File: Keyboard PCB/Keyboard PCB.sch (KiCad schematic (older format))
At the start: 15 parts

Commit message: Metidas las librerías acheron
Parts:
- added J?: USB_B_Mini, symbol Connector:USB_B_Mini
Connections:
- wire segments 52 -> 55
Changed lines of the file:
@@
 EESchema Schematic File Version 4
+LIBS:Keyboard PCB-cache
 EELAYER 30 0
 EELAYER END
@@
 Wire Wire Line
 	5250 1050 4900 1050
+$Comp
+L Connector:USB_B_Mini J?
+U 1 1 5D835ABB
+P 3500 1200
+F 0 "J?" H 3557 1667 50  0000 C CNN
+F 1 "USB_B_Mini" H 3557 1576 50  0000 C CNN
+F 2 "" H 3650 1150 50  0001 C CNN
+F 3 "~" H 3650 1150 50  0001 C CNN
+	1    3500 1200
+	1    0    0    -1
+$EndComp
+$Comp
+L power:+5V #PWR?
+U 1 1 5D837687
+P 3900 900
+F 0 "#PWR?" H 3900 750 50  0001 C CNN
+F 1 "+5V" H 3915 1073 50  0000 C CNN
+F 2 "" H 3900 900 50  0001 C CNN
+F 3 "" H 3900 900 50  0001 C CNN
+	1    3900 900
+	1    0    0    -1
+$EndComp
+Text GLabel 3800 1200 2    50   Input ~ 0
+D+
+Text GLabel 3800 1300 2    50   Input ~ 0
+D-
+Wire Wire Line
+	3800 1000 3900 1000
+Wire Wire Line
+	3900 1000 3900 900
+$Comp
+L power:GND #PWR?
+U 1 1 5D83AD54
+P 3500 1800
+F 0 "#PWR?" H 3500 1550 50  0001 C CNN
+F 1 "GND" H 3505 1627 50  0000 C CNN
+F 2 "" H 3500 1800 50  0001 C CNN
+F 3 "" H 3500 1800 50  0001 C CNN
+	1    3500 1800
+	1    0    0    -1
+$EndComp
+Wire Wire Line
+	3500 1600 3500 1800
 $EndSCHEMATC

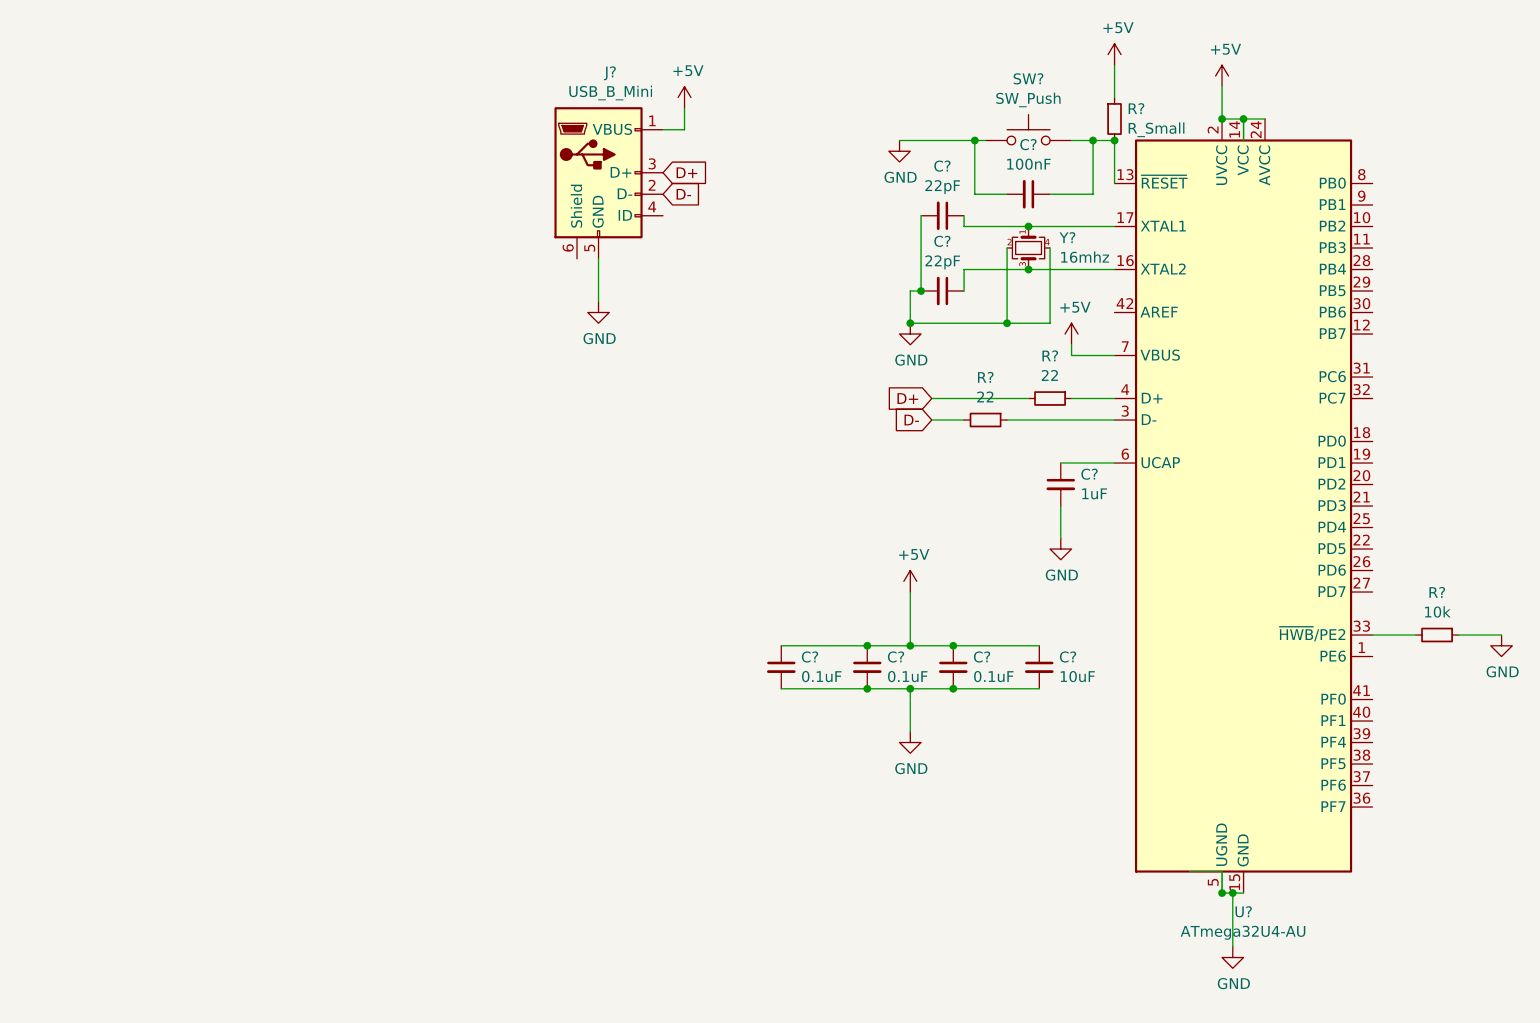
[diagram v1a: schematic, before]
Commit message: Añadida la librería de acheron
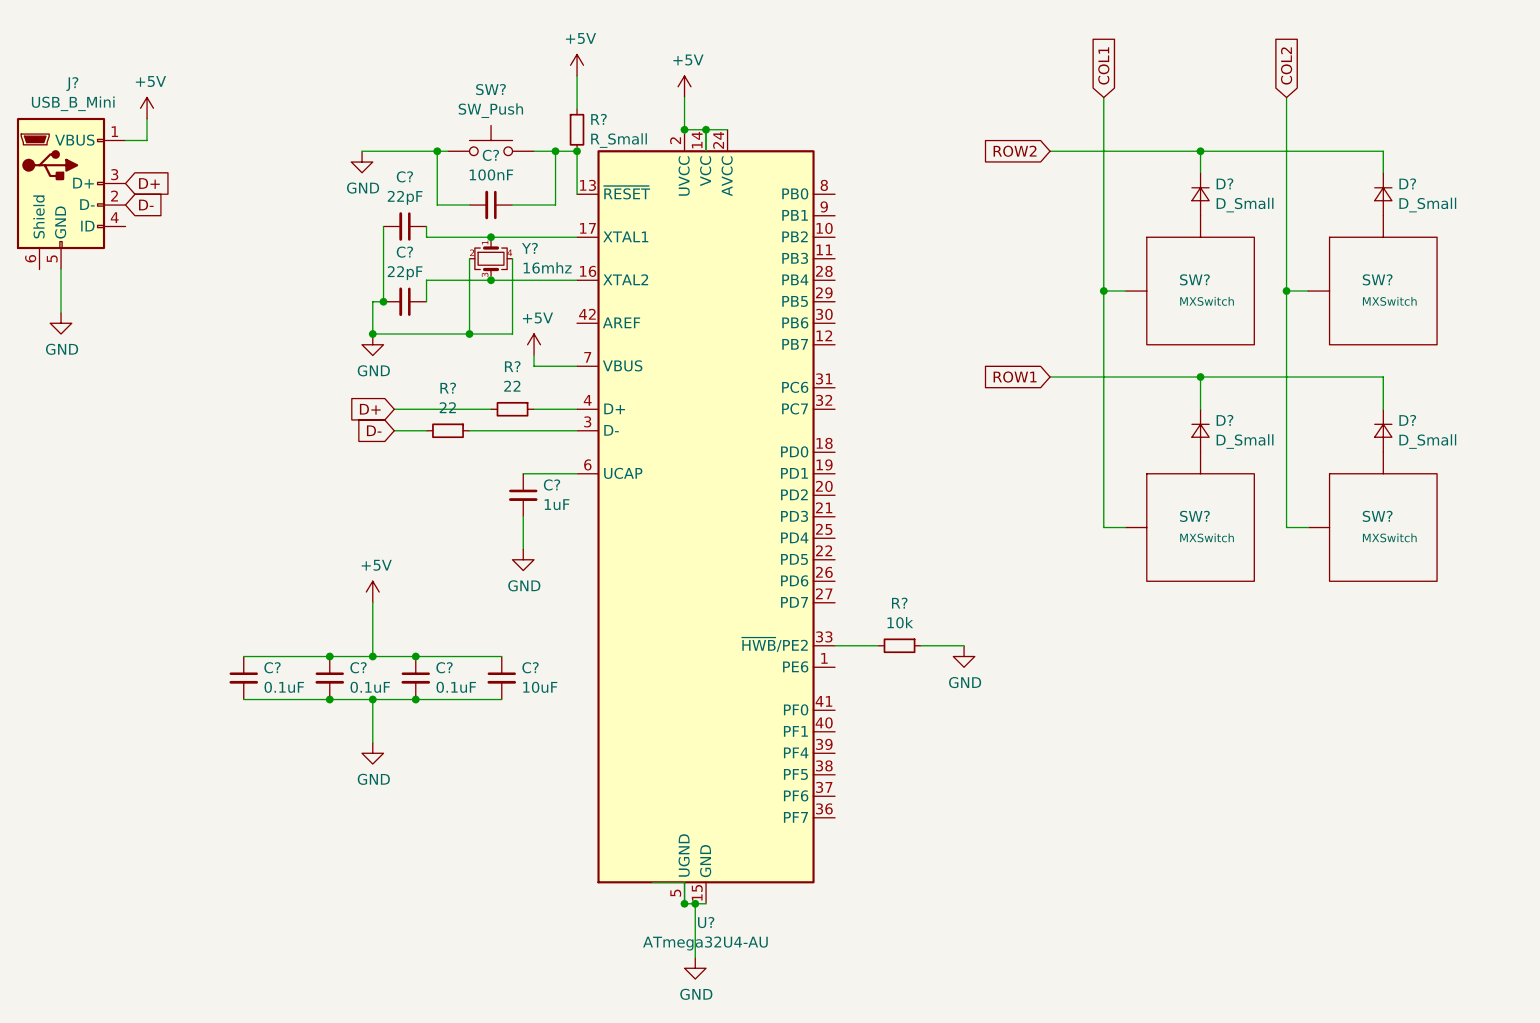
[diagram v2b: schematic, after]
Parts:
- added D? (x4): D_Small, symbol Device:D_Small
- added SW? (x4): MXSwitch, symbol acheronSymbols:MXSwitch
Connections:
- net labels added: COL1, COL2, ROW1, ROW2
- wire segments 55 -> 71
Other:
- moved on the sheet: C?, J?, R?, SW?, U?, Y?

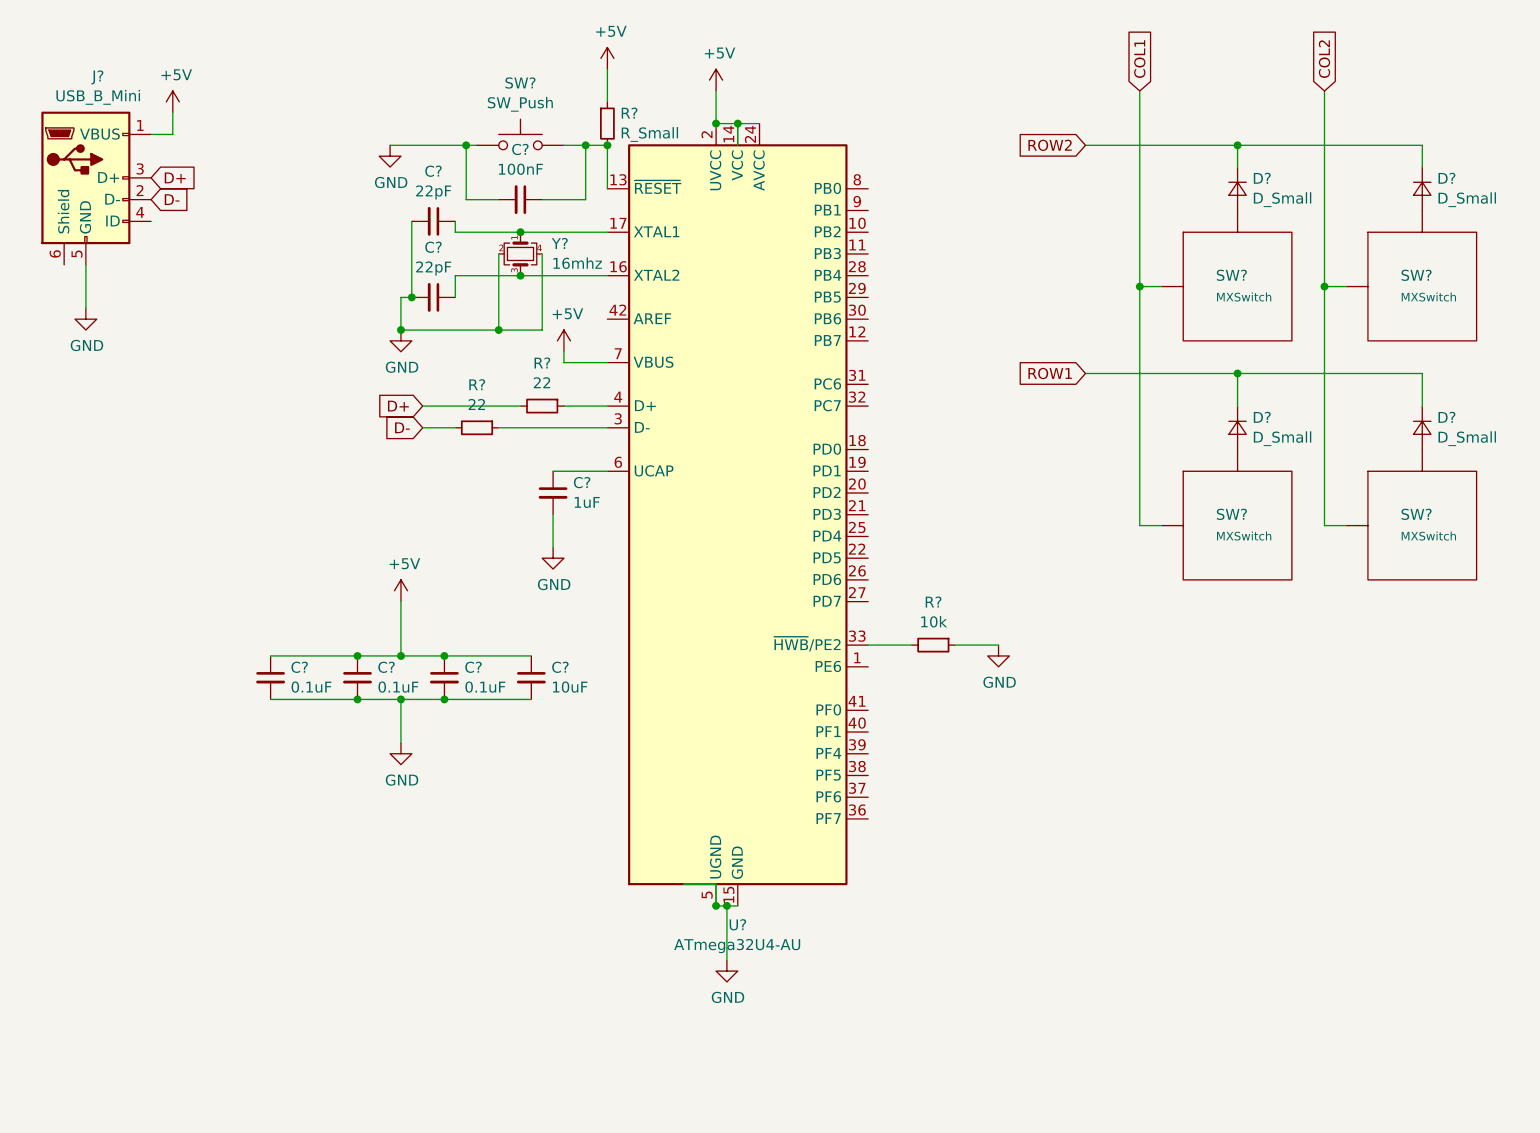
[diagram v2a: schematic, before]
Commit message: Aplicadas las Huellas
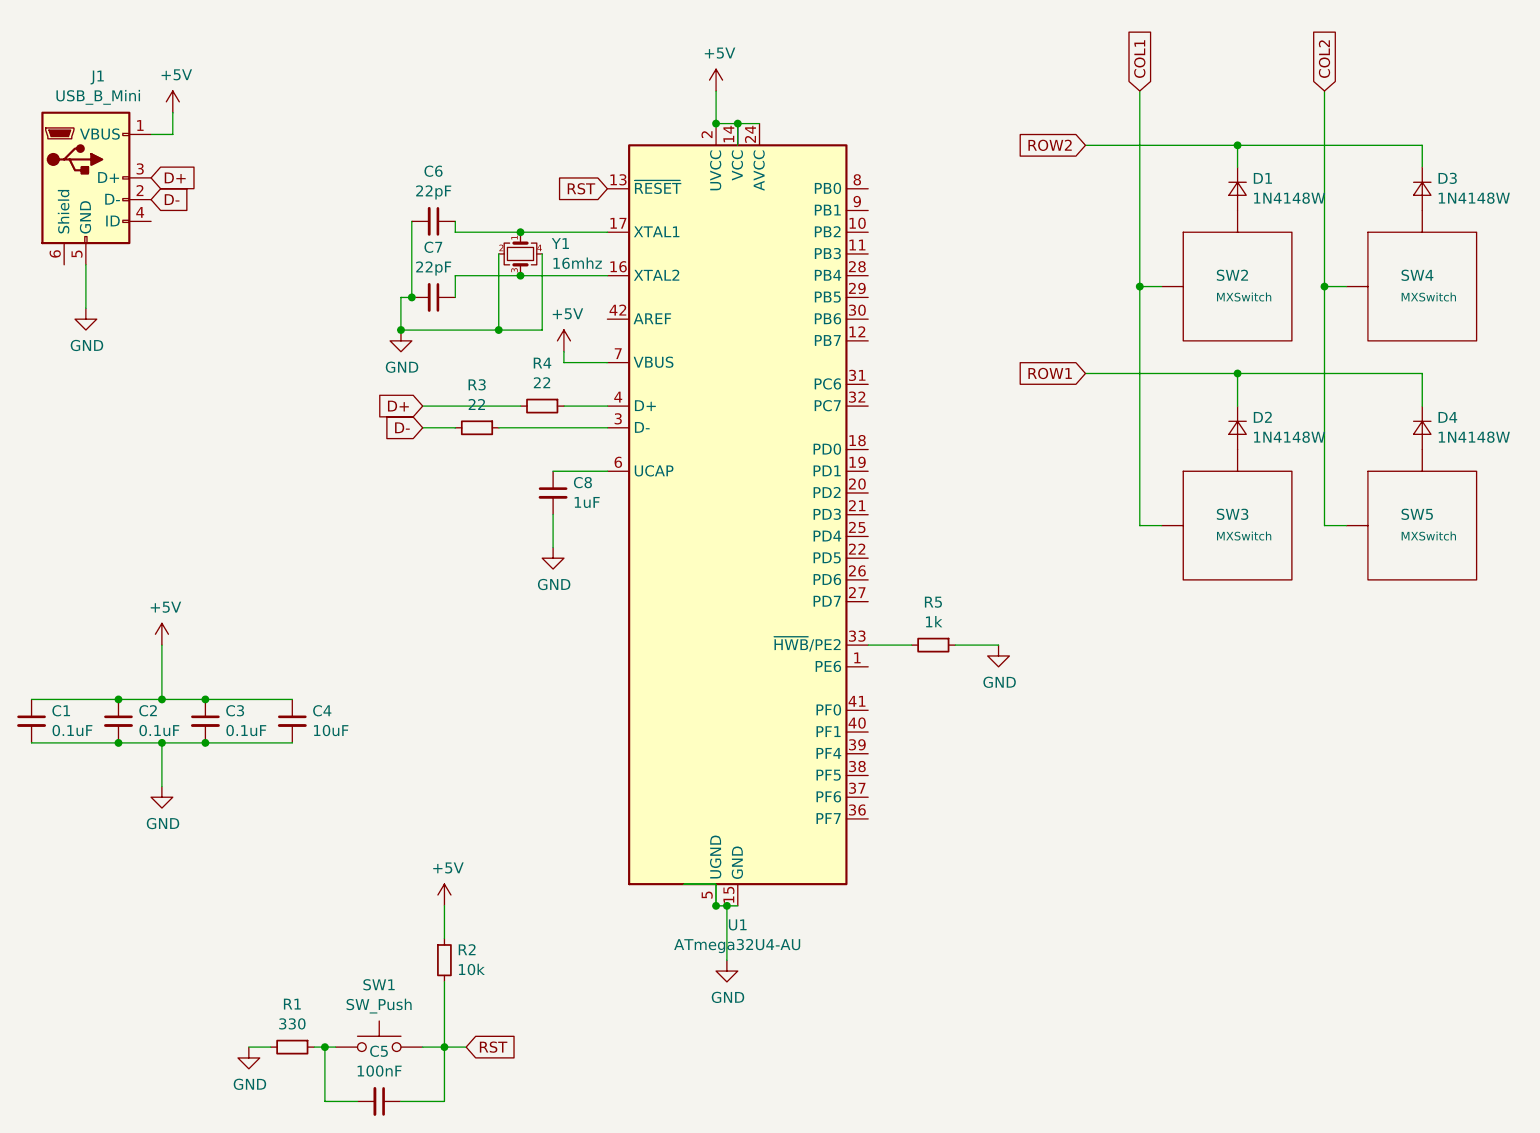
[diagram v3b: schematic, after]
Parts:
- removed D? (x3): D_Small, symbol Device:D_Small
- added D2, D3, D4: 1N4148W, Diode_SMD:D_SOD-123, symbol Device:D_Small
- added R1: 330, Resistor_SMD:R_1206_3216Metric_Pad1.42x1.75mm_HandSolder, symbol Device:R_Small
- C1, C2, C3, C4, C5, C6, C7, C8: renamed from C?; footprint (none) -> Diode_SMD:D_0805_2012Metric_Pad1.15x1.40mm_HandSolder
- D1: renamed from D?; value D_Small -> 1N4148W; footprint (none) -> Diode_SMD:D_SOD-123
- J1: renamed from J?; footprint (none) -> acheron_Connectors:USB_MiniB_XM7D-0512
- R2: renamed from R?; value R_Small -> 10k; footprint (none) -> Resistor_SMD:R_1206_3216Metric_Pad1.42x1.75mm_HandSolder
- R3, R4: renamed from R?; footprint (none) -> Resistor_SMD:R_1206_3216Metric_Pad1.42x1.75mm_HandSolder
- R5: renamed from R?; value 10k -> 1k; footprint (none) -> Resistor_SMD:R_1206_3216Metric_Pad1.42x1.75mm_HandSolder
- SW1, SW2, SW3, SW4: renamed from SW?; footprint (none) -> acheron_MX:MX100
- SW5: renamed from SW?; footprint (none) -> acheron_Hardware:smdPushBtn
- U1: renamed from U?; footprint Package_QFP:TQFP-44_10x10mm_P0.8mm -> acheron_Components:TQPF-44_10x10mm_P0.8mm
- Y1: renamed from Y?; footprint (none) -> Crystal:Crystal_SMD_3225-4Pin_3.2x2.5mm_HandSoldering
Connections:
- net labels added: RST
- wire segments 71 -> 72
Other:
- moved on the sheet: C1, C2, C3, C4, C5, R2, SW1

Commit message: Nombrando Switches
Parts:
- added D? (x75): 1N4148W, Diode_SMD:D_SOD-123, symbol Device:D_Small
- added SW?: ESC, acheron_MX:MX100, symbol acheronSymbols:MXSwitch
- added SW?: 1, acheron_MX:MX100, symbol acheronSymbols:MXSwitch
- added SW? (x49): MXSwitch, acheron_MX:MX100, symbol acheronSymbols:MXSwitch
- added SW? (x17): MXSwitch, acheron_Hardware:smdPushBtn, symbol acheronSymbols:MXSwitch
- added SW?: 2, acheron_MX:MX100, symbol acheronSymbols:MXSwitch
- added SW?: F5, acheron_MX:MX100, symbol acheronSymbols:MXSwitch
- added SW?: F6, acheron_MX:MX100, symbol acheronSymbols:MXSwitch
- added SW?: F7, acheron_MX:MX100, symbol acheronSymbols:MXSwitch
- added SW?: F8, acheron_Hardware:smdPushBtn, symbol acheronSymbols:MXSwitch
- added SW?: F9, acheron_MX:MX100, symbol acheronSymbols:MXSwitch
- added SW?: F10, acheron_Hardware:smdPushBtn, symbol acheronSymbols:MXSwitch
- SW2: value MXSwitch -> F1
- SW3: value MXSwitch -> F3
- SW4: value MXSwitch -> F2
- SW5: value MXSwitch -> F4
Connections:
- net labels added: COL10, COL11, COL12, COL13, COL14, COL15, COL16, COL17, COL18, COL19, COL20, COL3, COL4, COL5, COL6, COL7, COL8, COL9, ROW4
- wire segments 72 -> 372
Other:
- moved on the sheet: C1, C2, C3, C4, C5, C6, C7, C8, D1, D2, D3, D4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

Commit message: ROW2
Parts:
- added D?: 1N4148W, Diode_SMD:D_SOD-123, symbol Device:D_Small
- added SW?: F10, acheron_Hardware:smdPushBtn, symbol acheronSymbols:MXSwitch
- SW?: value MXSwitch -> Tab
- SW?: value MXSwitch -> Q
- SW?: value MXSwitch -> 3
- SW?: value MXSwitch -> W
- SW?: value MXSwitch -> E
- SW?: value MXSwitch -> 4
- SW?: value MXSwitch -> 5
- SW?: value MXSwitch -> R
- SW?: value MXSwitch -> T
- SW?: value MXSwitch -> 6
- SW? (x2): value MXSwitch -> 7
- SW?: value MXSwitch -> Y
- SW?: value MXSwitch -> U
- SW? (x2): value MXSwitch -> 8
- SW? (x2): value MXSwitch -> 9
- SW?: value MXSwitch -> I
- SW?: value MXSwitch -> O
- SW?: value MXSwitch -> 0
- SW? (x2): value MXSwitch -> -
- SW?: value MXSwitch -> P
- SW?: value MXSwitch -> [
- SW?: value MXSwitch -> =
- SW?: value MXSwitch -> Back Space
- SW?: value MXSwitch -> ]
- SW?: value MXSwitch -> \\
- SW?: value MXSwitch -> Num lock
- SW?: value MXSwitch -> /
- SW?: value MXSwitch -> *
- SW?: value MXSwitch -> +
- SW?: value MXSwitch -> A
- SW?: value MXSwitch -> S
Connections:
- wire segments 372 -> 373
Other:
- moved on the sheet: D?, SW?

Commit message: row 4
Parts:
- SW?: value MXSwitch -> D
- SW?: value MXSwitch -> F
- SW?: value MXSwitch -> G
- SW?: value MXSwitch -> H
- SW?: value MXSwitch -> J
- SW?: value MXSwitch -> K
- SW?: value MXSwitch -> L
- SW?: value MXSwitch -> ;
- SW?: value MXSwitch -> '
- SW? (x2): value MXSwitch -> Enter
- SW?: value MXSwitch -> 4
- SW?: value MXSwitch -> 5
- SW?: value MXSwitch -> 6
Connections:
- net labels added: ROW3
- wire segments 373 -> 369
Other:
- moved on the sheet: D?, SW?

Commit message: row 5
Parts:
- removed D?: 1N4148W, Diode_SMD:D_SOD-123, symbol Device:D_Small
- removed SW?: MXSwitch, acheron_Hardware:smdPushBtn, symbol acheronSymbols:MXSwitch
- added D? (x10): 1N4148W, Diode_SMD:D_SOD-123, symbol Device:D_Small
- added SW?: L Alt, acheron_Hardware:smdPushBtn, symbol acheronSymbols:MXSwitch
- added SW?: Space, acheron_Hardware:smdPushBtn, symbol acheronSymbols:MXSwitch
- added SW?: AltGr, acheron_Hardware:smdPushBtn, symbol acheronSymbols:MXSwitch
- added SW?: FN, acheron_Hardware:smdPushBtn, symbol acheronSymbols:MXSwitch
- added SW?: R Ctrl, acheron_Hardware:smdPushBtn, symbol acheronSymbols:MXSwitch
- added SW?: Left, acheron_Hardware:smdPushBtn, symbol acheronSymbols:MXSwitch
- added SW?: Down, acheron_Hardware:smdPushBtn, symbol acheronSymbols:MXSwitch
- added SW?: Right, acheron_Hardware:smdPushBtn, symbol acheronSymbols:MXSwitch
- added SW?: 0, acheron_Hardware:smdPushBtn, symbol acheronSymbols:MXSwitch
- added SW?: ., acheron_Hardware:smdPushBtn, symbol acheronSymbols:MXSwitch
- SW?: value F10 -> L Ctrl
- SW?: value MXSwitch -> L Shift
- SW?: value MXSwitch -> Z
- SW?: value MXSwitch -> X
- SW?: value MXSwitch -> C
- SW?: value MXSwitch -> V
- SW?: value MXSwitch -> B
- SW?: value MXSwitch -> N
- SW?: value MXSwitch -> M
- SW?: value MXSwitch -> ,
- SW?: value MXSwitch -> .
- SW?: value MXSwitch -> /
- SW?: value MXSwitch -> RShift
- SW?: value MXSwitch -> UP
- SW?: value MXSwitch -> 1
- SW?: value MXSwitch -> 2
- SW?: value MXSwitch -> 3
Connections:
- net labels added: ROW5
- wire segments 369 -> 412
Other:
- moved on the sheet: D?, SW?

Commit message: Asignadas huellas
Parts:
- SW1: footprint acheron_MX:MX100 -> acheron_Hardware:smdPushBtn
- SW10, SW11, SW17, SW25, SW27, SW33, SW35, SW42, SW44, SW50, SW52, SW53, SW55, SW59, SW61, SW67, SW69, SW71, SW72, SW73, SW79, SW80, SW82, SW87: renamed from SW?; footprint acheron_Hardware:smdPushBtn -> acheron_MX:MX100
- SW13: renamed from SW?; footprint acheron_MX:MX100 -> acheron_MX:MX150
- SW14, SW70: renamed from SW?; footprint acheron_MX:MX100 -> acheron_MX:MX225
- SW15, SW23, SW63: renamed from SW?; footprint acheron_Hardware:smdPushBtn -> acheron_MX:MX150
- SW40: renamed from SW?; footprint acheron_Hardware:smdPushBtn -> acheron_MX:MX625H
- SW5: footprint acheron_Hardware:smdPushBtn -> acheron_MX:MX100
- SW66: renamed from SW?; footprint acheron_MX:MX100 -> acheron_MX:MX175
- SW68: renamed from SW?; footprint acheron_MX:MX100 -> acheron_MX:MX200
- SW89: renamed from SW?; footprint acheron_Hardware:smdPushBtn -> acheron_MX:MX200V
- SW90: renamed from SW?; footprint acheron_MX:MX100 -> acheron_MX:MX200V
- gave numbers to parts that had none: 135
